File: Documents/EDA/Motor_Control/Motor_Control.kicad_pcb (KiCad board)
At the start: 2 copper layers, 58.4 x 71.1 mm, 8 parts, among them J1 V_MOTOR, M1 R, M2 Z

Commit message: libs and pcb and bom
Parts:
- removed A3: Adafruit_Feather_HUZZAH32_ESP32, Module:Adafruit_Feather
- added J2: Barrel_Jack, Connector_BarrelJack:BarrelJack_Horizontal, F.Cu at (213.0, 73.0)
- added U1: ESP32-DEVKITC-32D, MODULE_ESP32-DEVKITC-32D:MODULE_ESP32-DEVKITC-32D, F.Cu at (251.0, 96.0)
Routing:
- net +VDC: track 73.2 -> 0.00 mm
- net +3V3: track 69.8 -> 0.00 mm
- net Z_DIR: track 31.5 -> 0.00 mm
- net Z_STEP: track 30.6 -> 0.00 mm
- net R_DIR: track 30.6 -> 0.00 mm
- net R_STEP: track 30.0 -> 0.00 mm
- net Net-(A1-Pad5): track 12.3 -> 0.00 mm
- net Net-(A2-Pad6): track 12.3 -> 0.00 mm
- net Net-(A2-Pad5): track 12.3 -> 0.00 mm
- net Net-(A2-Pad4): track 12.3 -> 0.00 mm
- net Net-(A2-Pad3): track 12.3 -> 0.00 mm
- net Net-(A1-Pad6): track 12.3 -> 0.00 mm
- net Net-(A1-Pad4): track 12.3 -> 0.00 mm
- net Net-(A1-Pad3): track 12.3 -> 0.00 mm
- removed copper zone on B.Cu, net GND
- removed copper zone on F.Cu, net GNDD
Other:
- board outline removed

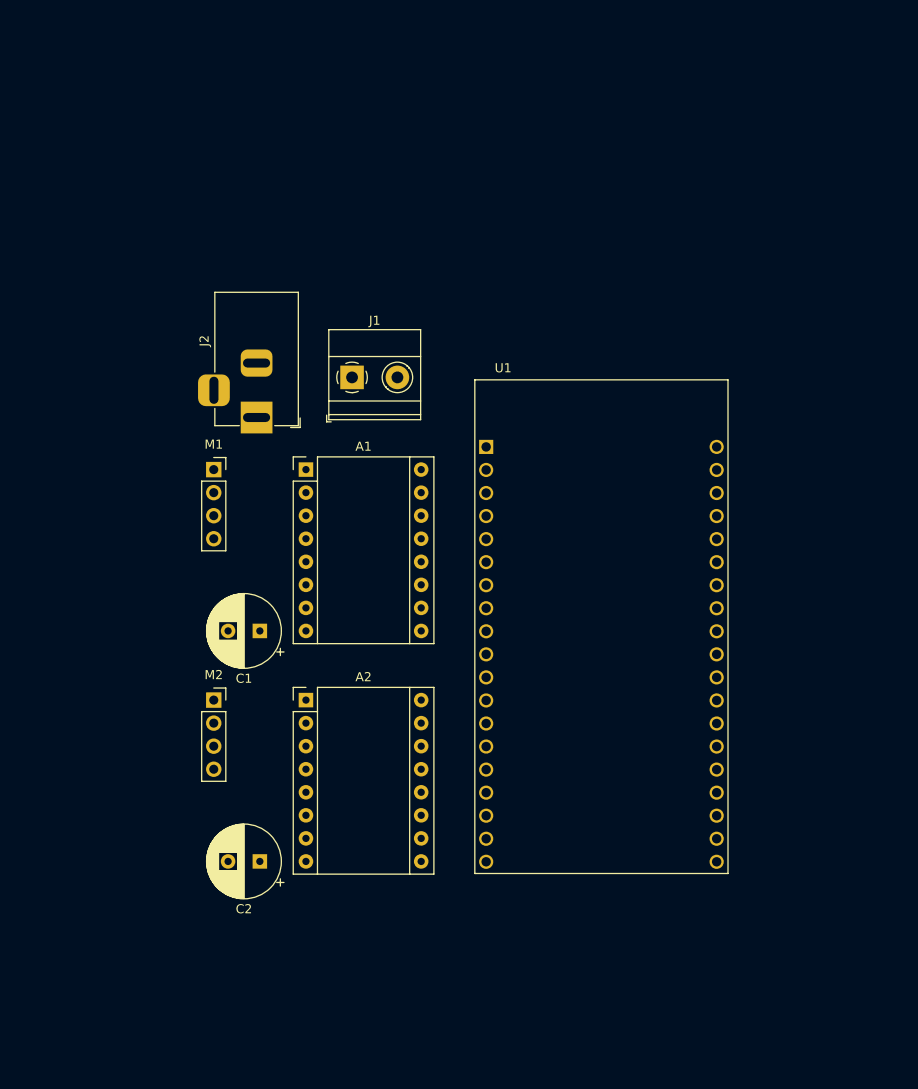
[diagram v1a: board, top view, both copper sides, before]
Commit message: connectors placed
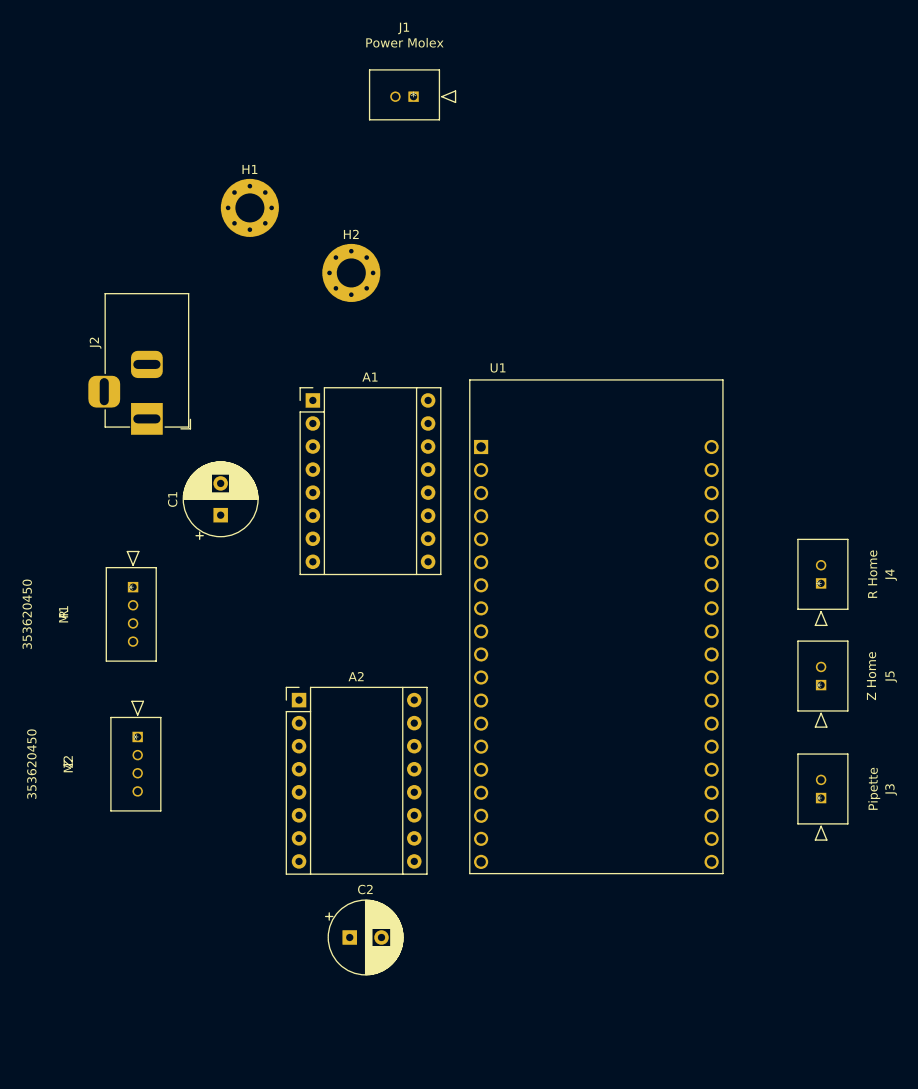
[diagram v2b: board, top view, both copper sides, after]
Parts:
- added H1: VDC, MountingHole:MountingHole_3.2mm_M3_Pad_Via, F.Cu at (212.3, 49.9)
- added H2: GND, MountingHole:MountingHole_3.2mm_M3_Pad_Via, F.Cu at (223.4, 57.1)
- added J3: Pipette, molex_sherlock:molex_sherlock_vrthdr_2pin, F.Cu at (275.2, 114.9)
- added J4: R Home, molex_sherlock:molex_sherlock_vrthdr_2pin, F.Cu at (275.2, 91.3)
- added J5: Z Home, molex_sherlock:molex_sherlock_vrthdr_2pin, F.Cu at (275.2, 102.5)
- J1: value V_MOTOR -> Power Molex; footprint TerminalBlock_Phoenix:TerminalBlock_Phoenix_MKDS-1,5-2_1x02_P5.00mm_Horizontal -> molex_sherlock:molex_sherlock_vrthdr_2pin
- M1, M2: footprint Connector_PinSocket_2.54mm:PinSocket_1x04_P2.54mm_Vertical -> molex_sherlock:molex_sherlock_4pin
- moved J1 31.7 mm to (230.3, 37.6)
- moved M1 15.7 mm to (199.4, 91.7), turned to 90 degrees
- moved C1 13.5 mm to (209.0, 83.8), turned to 90 degrees
- moved C2 13.0 mm to (223.3, 130.3), turned to 0 degrees
- moved J2 12.1 mm to (200.9, 73.2)
- moved M2 9.32 mm to (199.9, 108.2), turned to 90 degrees
- moved A1 7.66 mm to (219.2, 71.1)
- moved A2 0.76 mm to (217.7, 104.1)
- moved U1 0.56 mm to (250.4, 96.0)
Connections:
- A1 pad 15: R_STEP -> /R_STEP
- A1 pad 16: R_DIR -> /R_DIR
- A2 pad 15: Z_STEP -> /Z_STEP
- A2 pad 16: Z_DIR -> /Z_DIR
- J1 pad 1: +VDC -> GND
- J1 pad 2: GND -> +VDC
- U1 pad 1: Net-(U1-Pad1) -> +3V3
- U1 pad 14: Net-(U1-Pad14) -> GNDD
- U1 pad 20: Net-(U1-Pad20) -> GNDD
- U1 pad 21: Net-(U1-Pad21) -> /Z_STEP
- U1 pad 22: Net-(U1-Pad22) -> /Z_DIR
- U1 pad 26: Net-(U1-Pad26) -> GNDD
- U1 pad 27: Net-(U1-Pad27) -> /R_STEP
- U1 pad 28: Net-(U1-Pad28) -> /R_DIR
- U1 pad 30: Net-(U1-Pad30) -> /R_LIM
- U1 pad 31: Net-(U1-Pad31) -> /Z_LIM
- U1 pad 32: Net-(U1-Pad32) -> /PIP_TRIG

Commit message: Final pcb and bom
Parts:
- added H3: øM3, MountingHole:MountingHole_3.2mm_M3_Pad_Via, F.Cu at (201.0, 140.0)
- added H4: øM3, MountingHole:MountingHole_3.2mm_M3_Pad_Via, F.Cu at (201.0, 71.0)
- added H5: øM3, MountingHole:MountingHole_3.2mm_M3_Pad_Via, F.Cu at (259.0, 140.0)
- added H6: øM3, MountingHole:MountingHole_3.2mm_M3_Pad_Via, F.Cu at (259.0, 71.0)
- added J6: EXP, Connector_PinHeader_2.54mm:PinHeader_2x05_P2.54mm_Vertical, F.Cu at (221.0, 138.0)
- added TP1: Z_STEP, TestPoint:TestPoint_Pad_D1.0mm, F.Cu at (253.5, 91.5)
- added TP2: Z_DIR, TestPoint:TestPoint_Pad_D1.0mm, F.Cu at (253.5, 89.5)
- added TP3: R_STEP, TestPoint:TestPoint_Pad_D1.0mm, F.Cu at (253.5, 105.5)
- added TP4: R_DIR, TestPoint:TestPoint_Pad_D1.0mm, F.Cu at (253.5, 103.5)
- added TP5: PIP_TRIG, TestPoint:TestPoint_Pad_D1.0mm, F.Cu at (261.0, 125.0)
- added TP6: Z_LIM, TestPoint:TestPoint_Pad_D1.0mm, F.Cu at (261.0, 111.5)
- added TP7: R_LIM, TestPoint:TestPoint_Pad_D1.0mm, F.Cu at (261.0, 98.0)
- H1: value VDC -> +VDC; footprint MountingHole:MountingHole_3.2mm_M3_Pad_Via -> MountingHole:MountingHole_3.7mm_Pad_Via
- H2: footprint MountingHole:MountingHole_3.2mm_M3_Pad_Via -> MountingHole:MountingHole_3.7mm_Pad_Via
- J1: value Power Molex -> - Power +
- M1, M2: footprint molex_sherlock:molex_sherlock_4pin -> molex_sherlock:molex_sherlock_vrthdr_4pin
- moved C1 47.6 mm to (203.0, 131.0), turned to 180 degrees
- moved A1 44.2 mm to (208.3, 114.0)
- moved J1 42.0 mm to (211.0, 75.0), turned to 180 degrees
- moved J2 35.2 mm to (235.5, 80.0)
- moved C2 32.4 mm to (203.0, 105.0), turned to 180 degrees
- moved H2 29.6 mm to (247.0, 75.0)
- moved H1 26.9 mm to (222.0, 75.0)
- moved M1 24.4 mm to (201.0, 116.0)
- moved J3 19.4 mm to (257.5, 123.0), turned to 90 degrees
- moved J5 19.0 mm to (257.5, 109.5), turned to 90 degrees
- moved A2 18.5 mm to (208.3, 88.2)
- moved U1 18.4 mm to (238.4, 110.0)
- moved J4 18.3 mm to (257.5, 96.0), turned to 90 degrees
- moved M2 18.2 mm to (201.0, 90.0)
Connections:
- U1 pad 10: Net-(U1-Pad10) -> /IO26
- U1 pad 11: Net-(U1-Pad11) -> /IO27
- U1 pad 12: Net-(U1-Pad12) -> /IO14
- U1 pad 13: Net-(U1-Pad13) -> /IO12
- U1 pad 15: Net-(U1-Pad15) -> /IO13
- U1 pad 21: /Z_STEP -> /Z_DIR
- U1 pad 22: /Z_DIR -> /Z_STEP
- U1 pad 27: /R_STEP -> /R_DIR
- U1 pad 28: /R_DIR -> /R_STEP
- U1 pad 7: Net-(U1-Pad7) -> /IO32
- U1 pad 8: Net-(U1-Pad8) -> /IO33
- U1 pad 9: Net-(U1-Pad9) -> /IO25
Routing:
- net +VDC: track 0.00 -> 104.8 mm
- net /IO32: track 0.00 -> 59.0 mm, vias 0 -> 2
- net /IO33: track 0.00 -> 57.9 mm, vias 0 -> 1
- net +3V3: track 0.00 -> 55.7 mm
- net /IO25: track 0.00 -> 51.4 mm, vias 0 -> 2
- net GNDD: track 0.00 -> 47.8 mm, vias 0 -> 50
- net /IO14: track 0.00 -> 42.0 mm
- net /IO26: track 0.00 -> 41.2 mm, vias 0 -> 2
- net /IO27: track 0.00 -> 41.2 mm, vias 0 -> 1
- net /R_STEP: track 0.00 -> 38.8 mm
- net /R_DIR: track 0.00 -> 38.2 mm
- net /Z_STEP: track 0.00 -> 37.3 mm
- net /Z_DIR: track 0.00 -> 36.6 mm
- net /IO12: track 0.00 -> 35.4 mm
- net /IO13: track 0.00 -> 31.0 mm
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- added copper zone on B.Cu, net +VDC
- added copper zone on B.Cu, net GND
- added copper zone on F.Cu, net GND
- added copper zone on B.Cu, net GNDD
- added copper zone on F.Cu, net GNDD
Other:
- board outline added: 68 x 79 mm
- board text added: "Control Board Rev 1.0 Droplet Instrumentation Daniel Eisen : VUW ENGR489"
